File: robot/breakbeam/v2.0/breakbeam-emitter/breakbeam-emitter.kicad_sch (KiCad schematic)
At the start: 9 parts, among them J1 Conn_01x03, Q1 BSS138

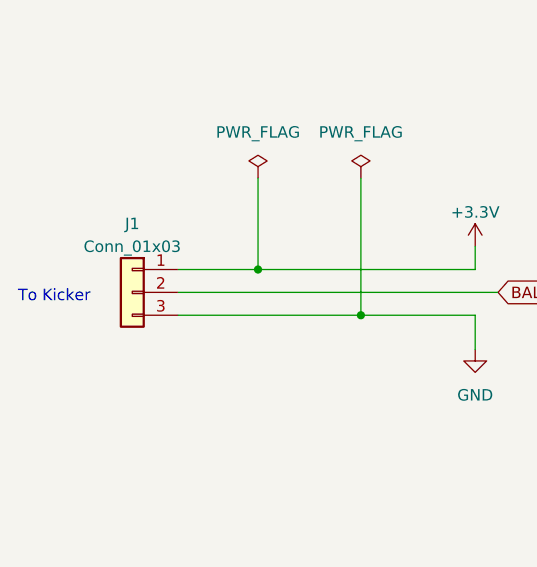
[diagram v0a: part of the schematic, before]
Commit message: Switch connector symbol to include MP
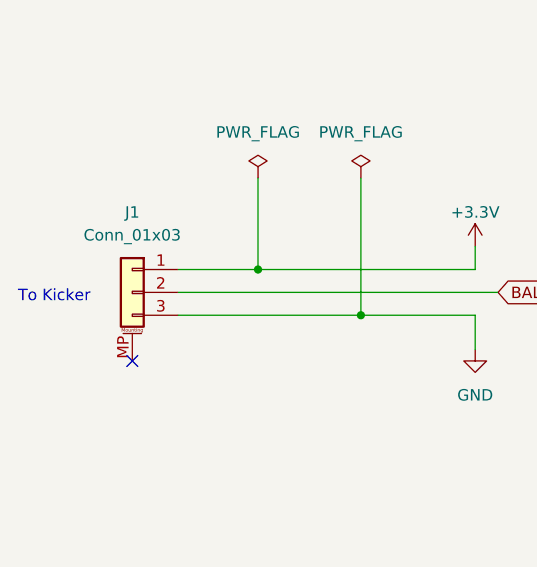
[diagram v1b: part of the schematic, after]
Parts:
- J1: footprint Connector_JST:JST_SH_SM03B-SRSS-TB_1x03-1MP_P1.00mm_Horizontal -> Connector_JST:JST_GH_SM03B-GHS-TB_1x03-1MP_P1.25mm_Horizontal; symbol Connector_Generic:Conn_01x03 -> Connector_Generic_MountingPin:Conn_01x03_MountingPin
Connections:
- no-connect marks 1 -> 2

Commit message: Update LCSC part number
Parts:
- J1: LCSC C160403 -> C514175
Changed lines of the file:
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@@
 			)
 		)
-		(property "LCSC" "C160403"
+		(property "LCSC" "C514175"
 			(at 81.28 97.79 0)
 			(effects
